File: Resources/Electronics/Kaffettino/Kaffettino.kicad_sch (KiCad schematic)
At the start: 36 parts, among them J2 OSTVN02A150, J3 OSTVN04A150, J4 OSTVN04A150, J5 OSTVN04A150, M1 RFID-RC522, U1 PCF8574AN, U2 DFR0299, U3 ESP32-38Pin-Wroom, U4 26052

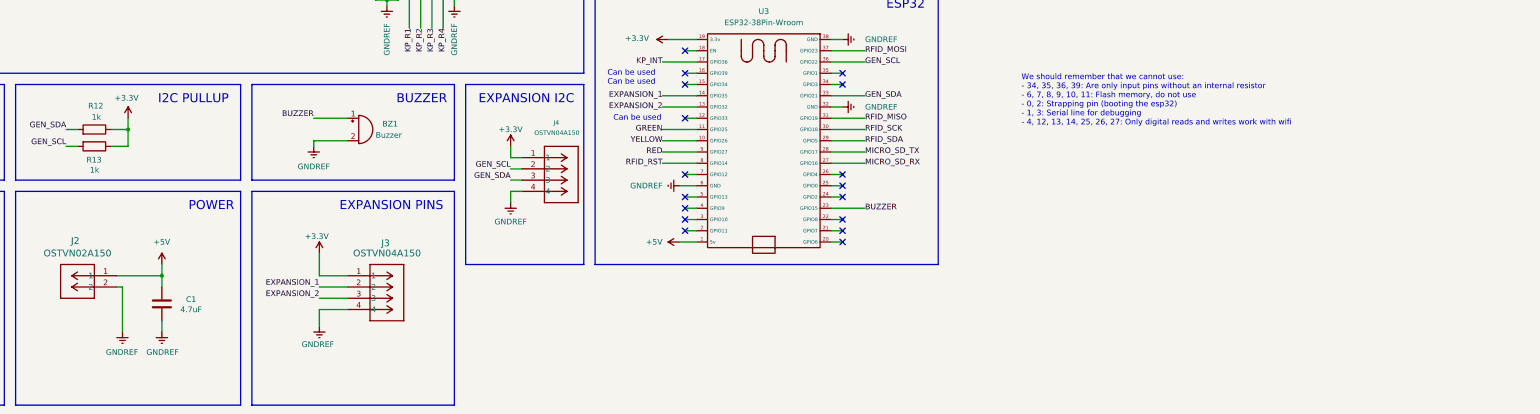
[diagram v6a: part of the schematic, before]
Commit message: Embedded: Finished developing PCB, fixed grb and drill files, added silkscreen.
TODO: Check correctness of footprints and NPN Junction.
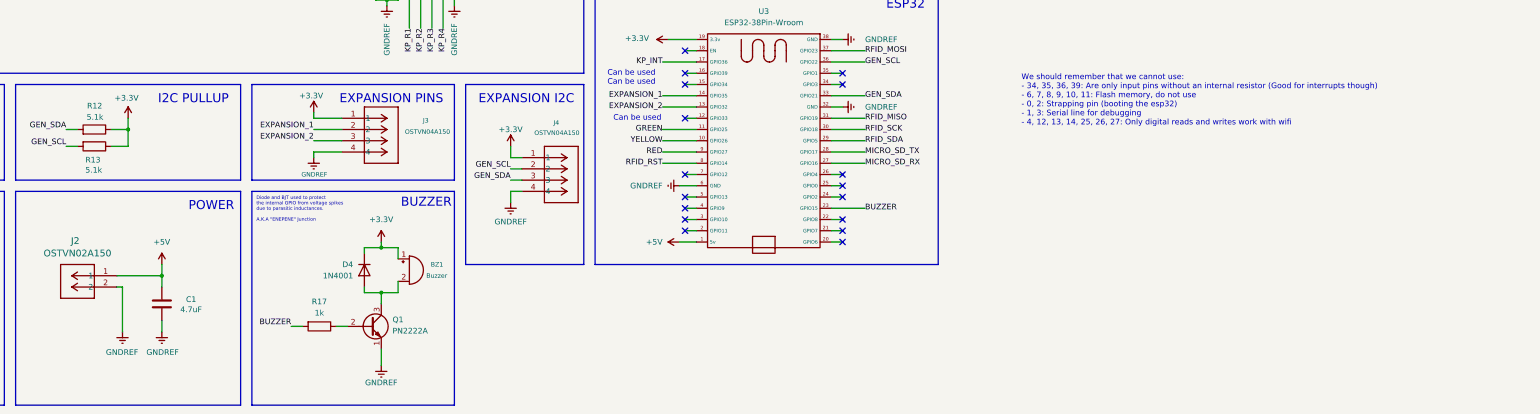
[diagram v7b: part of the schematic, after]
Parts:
- added D4: 1N4001, Diode_THT:D_DO-41_SOD81_P10.16mm_Horizontal, symbol Diode:1N4001
- added Q1: PN2222A, Package_TO_SOT_THT:TO-92_Inline, symbol Transistor_BJT:PN2222A
- added R17: 1k, Resistor_THT:R_Axial_DIN0207_L6.3mm_D2.5mm_P10.16mm_Horizontal, symbol Device:R
- R12, R13: value 1k -> 5.1k
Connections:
- net +3.3V: now also BZ1.1 (+), D4.1 (K)
- net BUZZER: now also R17.2; no longer BZ1.1 (+)
- net GNDREF: now also Q1.1 (E); no longer BZ1.2 (-)
- new net: BZ1.2 (-), D4.2 (A), Q1.3 (C)
- new net: Q1.2 (B), R17.1
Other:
- note added: "Diode and BJT used to protect the internal GPIO from voltage spikes due to parasitic inductances. A.K.A "ENEPENE" Junction"
- note added: "We should remember that we cannot use: - 34, 35, 36, 39: Are only input pins without an internal resistor (Good for interrupts though) - 6, 7, 8, 9, 10, 11: Flash memory, do not use - 0, 2: Strapping pin (booting the esp32) - 1, 3: Serial line for debugging - 4, 12, 13, 14, 25, 26, 27: Only digital reads and writes work with wifi"
- note removed: "We should remember that we cannot use: - 34, 35, 36, 39: Are only input pins without an internal resistor - 6, 7, 8, 9, 10, 11: Flash memory, do not use - 0, 2: Strapping pin (booting the esp32) - 1, 3: Serial line for debugging - 4, 12, 13, 14, 25, 26, 27: Only digital reads and writes work with wifi"
- moved on the sheet: BZ1, J3

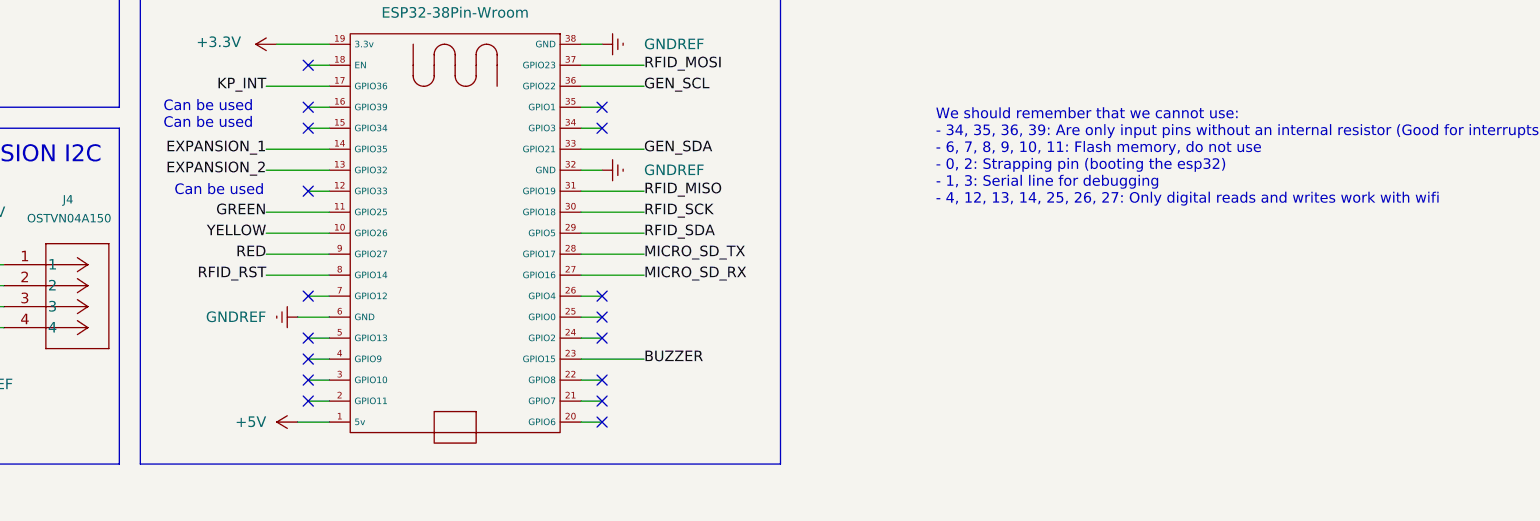
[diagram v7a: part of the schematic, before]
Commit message: Embedded: Switched buzzer from 15 (strapping pin) to 33, reflected the changes in the PCB
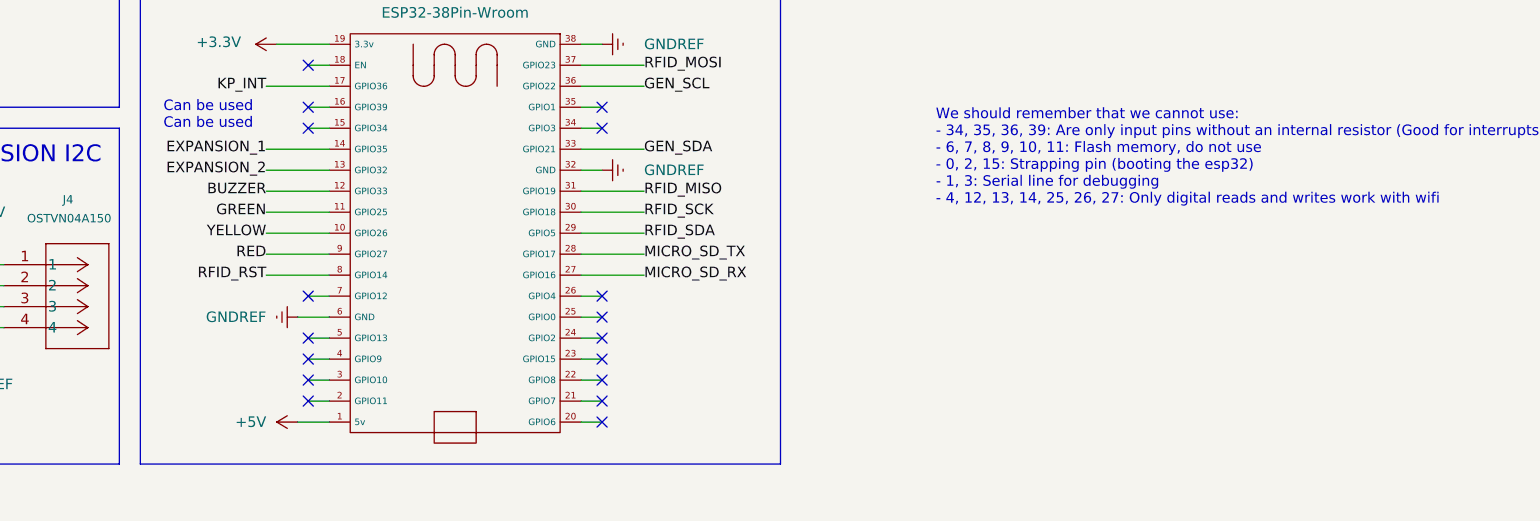
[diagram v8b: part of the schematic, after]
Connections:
- net BUZZER: now also U3.12 (GPIO33); no longer U3.23 (GPIO15)
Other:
- note added: "We should remember that we cannot use: - 34, 35, 36, 39: Are only input pins without an internal resistor (Good for interrupts though) - 6, 7, 8, 9, 10, 11: Flash memory, do not use - 0, 2, 15: Strapping pin (booting the esp32) - 1, 3: Serial line for debugging - 4, 12, 13, 14, 25, 26, 27: Only digital reads and writes work with wifi"
- note removed: "We should remember that we cannot use: - 34, 35, 36, 39: Are only input pins without an internal resistor (Good for interrupts though) - 6, 7, 8, 9, 10, 11: Flash memory, do not use - 0, 2: Strapping pin (booting the esp32) - 1, 3: Serial line for debugging - 4, 12, 13, 14, 25, 26, 27: Only digital reads and writes work with wifi"
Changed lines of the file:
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@@
-		)
-	)
-	(text "Can be used"
-		(exclude_from_sim no)
-		(at 220.726 130.81 0)
-		(effects
-			(font
-				(size 1.27 1.27)
-			)
-			(justify right)
 		)
 	)
@@
 		)
 	)
-	(text "We should remember that we cannot use:\n- 34, 35, 36, 39: Are only input pins without an internal resistor (Good for interrupts though)\n- 6, 7, 8, 9, 10, 11: Flash memory, do not use\n- 0, 2: Strapping pin (booting the esp32)\n- 1, 3: Serial line for debugging\n- 4, 12, 13, 14, 25, 26, 27: Only digital reads and writes work with wifi"
+	(text "We should remember that we cannot use:\n- 34, 35, 36, 39: Are only input pins without an internal resistor (Good for interrupts though)\n- 6, 7, 8, 9, 10, 11: Flash memory, do not use\n- 0, 2, 15: Strapping pin (booting the esp32)\n- 1, 3: Serial line for debugging\n- 4, 12, 13, 14, 25, 26, 27: Only digital reads and writes work with wifi"
 		(exclude_from_sim no)
 		(at 302.006 126.746 0)
@@
 	)
 	(no_connect
+		(at 261.62 151.13)
+	)
+	(no_connect
 		(at 226.06 143.51)
 	)
@@
 	)
 	(no_connect
-		(at 226.06 130.81)
-	)
-	(no_connect
 		(at 261.62 143.51)
 	)
@@
 	(wire
 		(pts
+			(xy 261.62 151.13) (xy 259.08 151.13)
+		)
+		(stroke
+			(width 0)
+			(type default)
+		)
+	)
+	(wire
+		(pts
 			(xy 259.08 113.03) (xy 261.62 113.03)
 		)
@@
 	(wire
 		(pts
-			(xy 259.08 151.13) (xy 266.7 151.13)
-		)
-		(stroke
-			(width 0)
-			(type default)
-		)
-	)
-	(wire
-		(pts
 			(xy 27.94 181.61) (xy 27.94 184.15)
 		)
@@
 	(wire
 		(pts
-			(xy 226.06 130.81) (xy 228.6 130.81)
-		)
-		(stroke
-			(width 0)
-			(type default)
-		)
-	)
-	(wire
-		(pts
 			(xy 43.18 181.61) (xy 43.18 184.15)
 		)
@@
 		(pts
 			(xy 31.75 134.62) (xy 43.18 134.62)
+		)
+		(stroke
+			(width 0)
+			(type default)
+		)
+	)
+	(wire
+		(pts
+			(xy 220.98 130.81) (xy 228.6 130.81)
 		)
 		(stroke
@@
 	)
 	(label "BUZZER"
-		(at 266.7 151.13 0)
+		(at 220.98 130.81 180)
 		(effects
 			(font
@@
 				(color 0 0 0 1)
 			)
-			(justify left)
-		)
-	)
+			(justify right)
+		)
+	)
